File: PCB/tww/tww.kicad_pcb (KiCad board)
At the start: 2 copper layers, 77 x 77 mm, 56 parts, among them J1 MAINS, J10 Flow|NTC, J11 SPI, J2 WW_Pump, J3 Circ_Pump, J6 FtdiConnector, J9 1Wire Sensors, Q1 BC547, Q2 BC547, SW1 Reset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

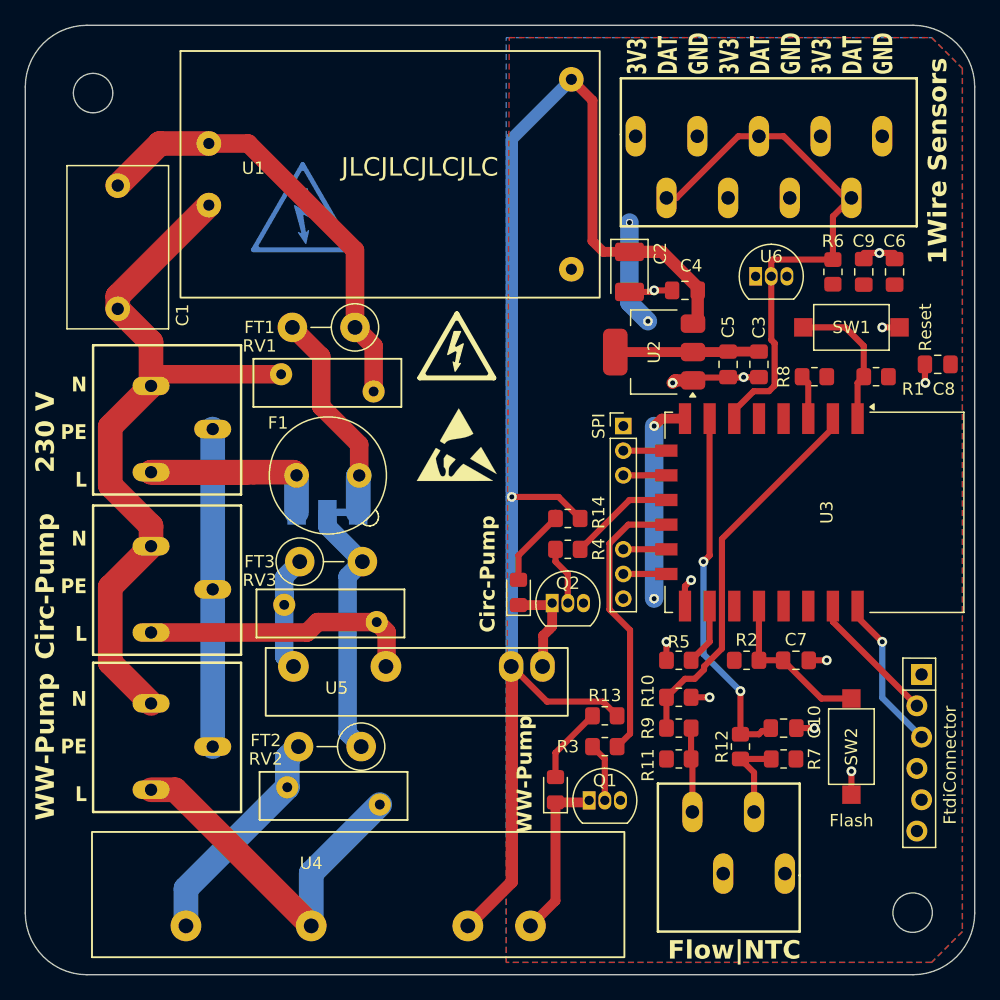
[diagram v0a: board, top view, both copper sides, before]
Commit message: update to PCB v1.1
addresses #1

- U1 (HLK-PM01) output polarity swapped
- J6 (FtdiConnector): RX and TX swapped
- J10 label fixed
- VDR-0.6 footprint changed
- replaced BC547 by FET IRLML6344
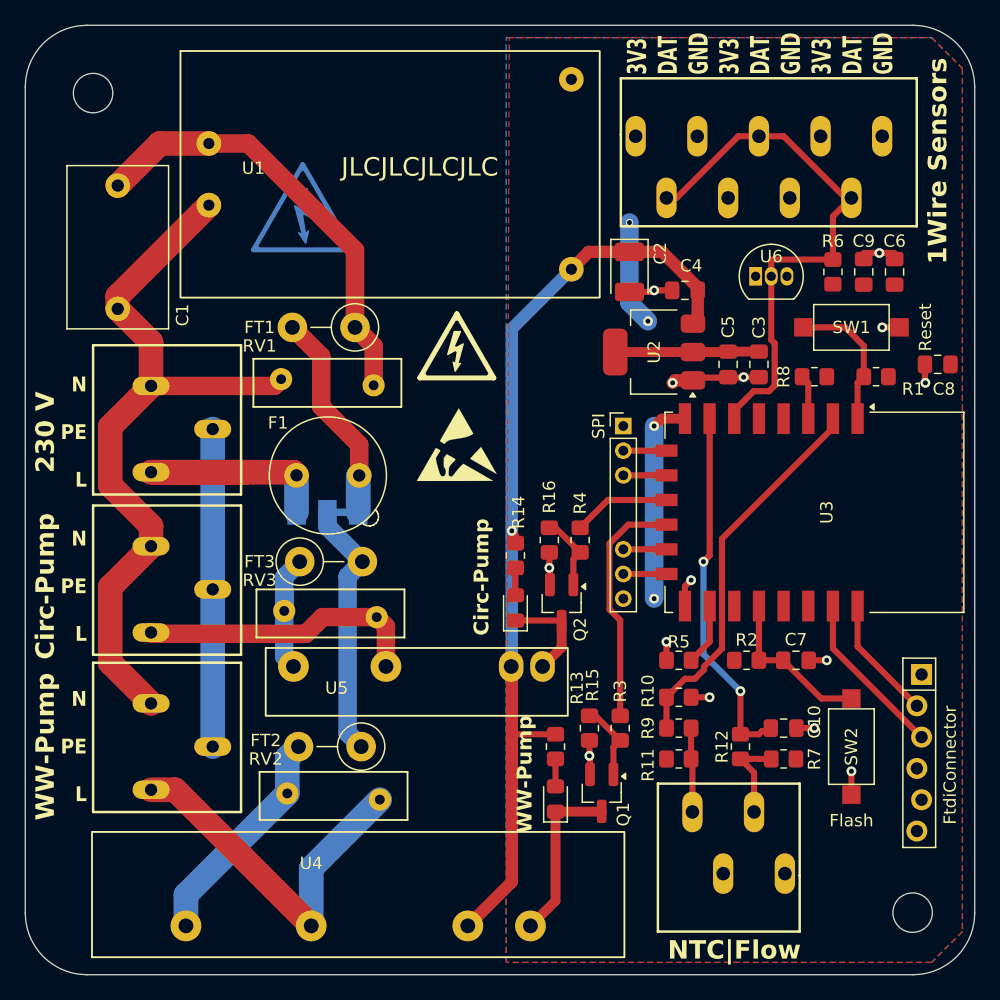
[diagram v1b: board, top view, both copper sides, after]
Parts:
- added R15: 10k, Resistor_SMD:R_0805_2012Metric_Pad1.20x1.40mm_HandSolder, F.Cu at (145.8, 81.0)
- added R16: 10k, Resistor_SMD:R_0805_2012Metric_Pad1.20x1.40mm_HandSolder, F.Cu at (142.5, 65.8)
- J10: value Flow|NTC -> NTC|Flow
- Q1, Q2: value BC547 -> IRLML6344; footprint Package_TO_SOT_THT:TO-92_Inline -> Package_TO_SOT_SMD:SOT-23_Handsoldering
- R13, R14: value 1k? -> 560
- R3, R4: value 1k? -> 300
- moved R14 5.20 mm to (139.8, 67.0), turned to 90 degrees
- moved R13 4.72 mm to (143.0, 82.5), turned to 90 degrees
- moved R3 1.95 mm to (148.2, 81.0), turned to -90 degrees
- moved D2 1.27 mm to (139.8, 71.2)
- moved R4 1.25 mm to (145.0, 65.8), turned to -90 degrees
- moved Q1 1.19 mm to (146.8, 86.2), turned to -90 degrees
- moved Q2 0.77 mm to (143.5, 70.9), turned to -90 degrees
- moved D1 0.75 mm to (143.0, 86.8)
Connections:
- J6 pad 2: /RX -> /TX
- J6 pad 3: /TX -> /RX
- Q1 pad 1: Net-(D1-K) -> Net-(Q1-G)
- Q1 pad 2: Net-(Q1-B) -> GND
- Q1 pad 3: GND -> Net-(D1-K)
- Q2 pad 1: Net-(D2-K) -> Net-(Q2-G)
- Q2 pad 2: Net-(Q2-B) -> GND
- Q2 pad 3: GND -> Net-(D2-K)
- R3 pad 2: Net-(Q1-B) -> Net-(Q1-G)
- R4 pad 2: Net-(Q2-B) -> Net-(Q2-G)
- U1 pad 3: +5V -> GND
- U1 pad 4: GND -> +5V
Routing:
- net +5V: track 115.6 -> 76.6 mm
- net Net-(Q1-G): track 0.00 -> 6.31 mm
- net Net-(Q2-G): track 0.00 -> 6.17 mm
- net GND: track 26.3 -> 31.7 mm, vias 12 -> 14
- net Net-(Q2-B): track 4.77 -> 0.00 mm
- net Net-(Q1-B): track 4.77 -> 0.00 mm
- net Net-(D2-A): track 6.69 -> 2.22 mm
- net Net-(D1-A): track 6.22 -> 2.22 mm
- net /WWP: track 22.9 -> 19.6 mm
- net /TX: track 12.8 -> 10.1 mm, vias 1 -> 0
- net /RX: track 10.9 -> 13.6 mm
- net /L_CIRC: track 22.6 -> 23.4 mm
- net /CIRC: track 8.66 -> 7.93 mm
- net Net-(D1-K): track 13.2 -> 13.9 mm
- net Net-(U1-AC1): track 36.3 -> 35.8 mm
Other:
- board text added: "stan23 10/2024 v1.1 CC BY-NC-SA"
- board text removed: "stan23 10/2024 v1.0 CC BY-NC-SA"

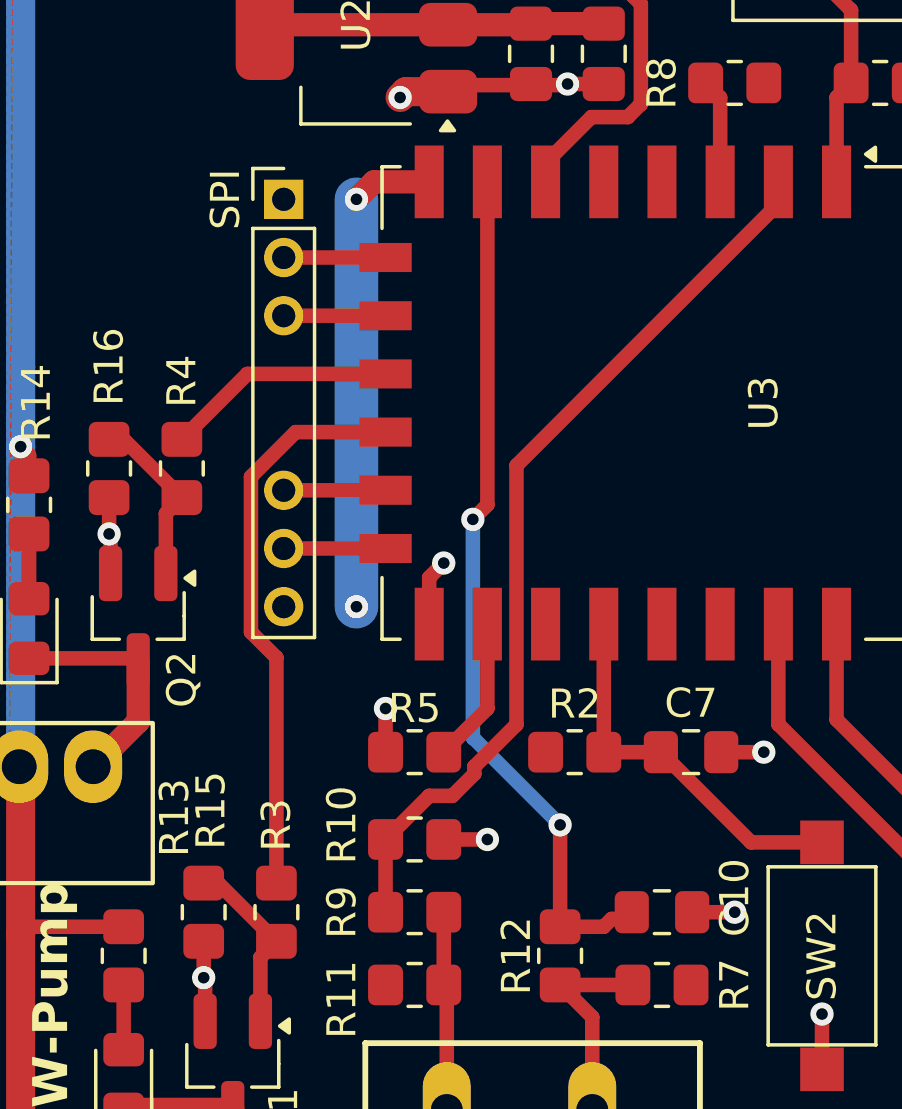
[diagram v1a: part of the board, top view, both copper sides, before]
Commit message: updates for PCB version 1.1
- reconnect WWP and CIRC outputs
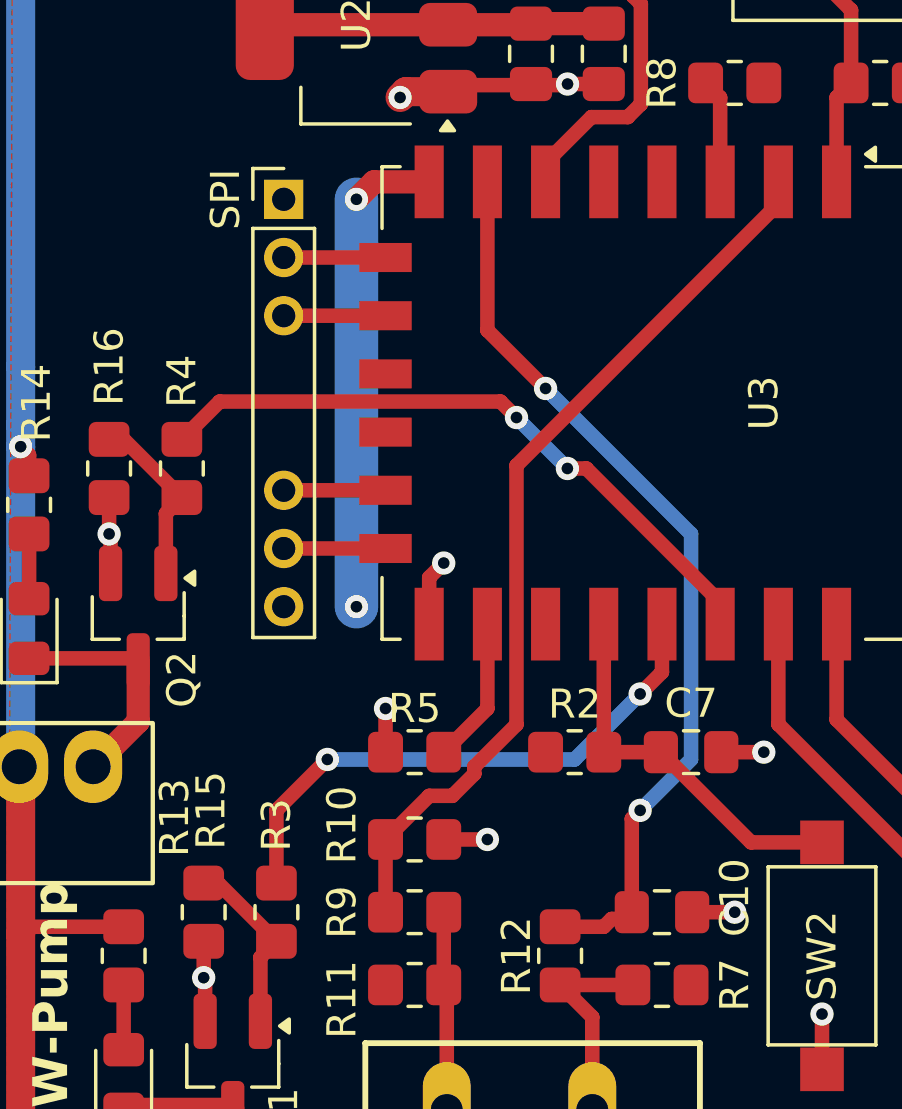
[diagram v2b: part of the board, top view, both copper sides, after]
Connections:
- U3 pad 11: /CIRC -> unconnected-(U3-GPIO9-Pad11)
- U3 pad 12: /WWP -> unconnected-(U3-GPIO10-Pad12)
- U3 pad 19: unconnected-(U3-GPIO4-Pad19) -> /WWP
- U3 pad 20: unconnected-(U3-GPIO5-Pad20) -> /CIRC
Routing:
- net /CIRC: track 7.93 -> 22.6 mm, vias 0 -> 2
- net /FLOW: track 29.7 -> 31.5 mm
- net /WWP: track 19.6 -> 19.4 mm, vias 0 -> 2
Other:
- board text added: "stan23 11/2024 v1.1 CC BY-NC-SA"
- board text removed: "stan23 10/2024 v1.1 CC BY-NC-SA"
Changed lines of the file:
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@@
 	(net 37 "unconnected-(U3-GPIO2-Pad17)")
 	(net 38 "Net-(J10-Pin_2)")
-	(net 39 "unconnected-(U3-GPIO4-Pad19)")
-	(net 40 "unconnected-(U3-GPIO5-Pad20)")
+	(net 39 "unconnected-(U3-GPIO10-Pad12)")
+	(net 40 "unconnected-(U3-GPIO9-Pad11)")
 	(net 41 "/L_SSR")
 	(net 42 "Net-(Q1-G)")
@@
 			(size 1 1.8)
 			(layers "F.Cu" "F.Paste" "F.Mask")
-			(net 10 "/CIRC")
+			(net 40 "unconnected-(U3-GPIO9-Pad11)")
 			(pinfunction "GPIO9")
-			(pintype "bidirectional")
+			(pintype "bidirectional+no_connect")
 		)
 		(pad "12" smd rect
@@
 			(size 1 1.8)
 			(layers "F.Cu" "F.Paste" "F.Mask")
-			(net 9 "/WWP")
+			(net 39 "unconnected-(U3-GPIO10-Pad12)")
 			(pinfunction "GPIO10")
-			(pintype "bidirectional")
+			(pintype "bidirectional+no_connect")
 		)
 		(pad "13" smd rect
@@
 			(size 2.5 1)
 			(layers "F.Cu" "F.Paste" "F.Mask")
-			(net 39 "unconnected-(U3-GPIO4-Pad19)")
+			(net 9 "/WWP")
 			(pinfunction "GPIO4")
-			(pintype "bidirectional+no_connect")
+			(pintype "bidirectional")
 		)
 		(pad "20" smd rect
@@
 			(size 2.5 1)
 			(layers "F.Cu" "F.Paste" "F.Mask")
-			(net 40 "unconnected-(U3-GPIO5-Pad20)")
+			(net 10 "/CIRC")
 			(pinfunction "GPIO5")
-			(pintype "bidirectional+no_connect")
+			(pintype "bidirectional")
 		)
 		(pad "21" smd rect
@@
 		(layer "User.1")
 	)
-	(gr_text "stan23   10/2024   v1.1\nCC BY-NC-SA"
+	(gr_text "stan23   11/2024   v1.1\nCC BY-NC-SA"
 		(at 145.25 48 90)
 		(layer "B.SilkS")
@@
 	)
 	(segment
-		(start 147.375 71.375)
-		(end 147.375 66.034009)
+		(start 148.25 80)
+		(end 148.25 77.5)
 		(width 0.5)
 		(layer "F.Cu")
@@
 	)
 	(segment
-		(start 148.25 72.25)
-		(end 147.375 71.375)
+		(start 161.5 71.1)
+		(end 161.5 72.75)
 		(width 0.5)
 		(layer "F.Cu")
@@
 	)
 	(segment
-		(start 147.375 66.034009)
-		(end 148.909009 64.5)
+		(start 150 75.75)
+		(end 148.25 77.5)
 		(width 0.5)
 		(layer "F.Cu")
@@
 	)
 	(segment
-		(start 148.25 80)
-		(end 148.25 72.25)
+		(start 161.5 72.75)
+		(end 160.75 73.5)
 		(width 0.5)
 		(layer "F.Cu")
 		(net 9)
 	)
+	(via
+		(at 150 75.75)
+		(size 0.8)
+		(drill 0.4)
+		(layers "F.Cu" "B.Cu")
+		(net 9)
+	)
+	(via
+		(at 160.75 73.5)
+		(size 0.8)
+		(drill 0.4)
+		(layers "F.Cu" "B.Cu")
+		(net 9)
+	)
 	(segment
-		(start 148.909009 64.5)
-		(end 152 64.5)
+		(start 158.5 75.75)
+		(end 150 75.75)
 		(width 0.5)
-		(layer "F.Cu")
+		(layer "B.Cu")
+		(net 9)
+	)
+	(segment
+		(start 160.75 73.5)
+		(end 158.5 75.75)
+		(width 0.5)
+		(layer "B.Cu")
 		(net 9)
 	)
 	(segment
-		(start 145 64.75)
-		(end 147.25 62.5)
+		(start 155.95 63.45)
+		(end 146.3 63.45)
+		(width 0.5)
+		(layer "F.Cu")
+		(net 10)
+	)
+	(segment
+		(start 158.9 65.75)
+		(end 158.25 65.75)
+		(width 0.5)
+		(layer "F.Cu")
+		(net 10)
+	)
+	(segment
+		(start 146.3 63.45)
+		(end 145 64.75)
 		(width 0.5)
 		(layer "F.Cu")
@@
 	)
 	(segment
-		(start 147.25 62.5)
-		(end 152 62.5)
+		(start 156.5 64)
+		(end 155.95 63.45)
 		(width 0.5)
 		(layer "F.Cu")
@@
 	)
 	(segment
+		(start 163.5 71.1)
+		(end 163.5 70.35)
+		(width 0.5)
+		(layer "F.Cu")
+		(net 10)
+	)
+	(segment
+		(start 163.5 70.35)
+		(end 158.9 65.75)
+		(width 0.5)
+		(layer "F.Cu")
+		(net 10)
+	)
+	(via
+		(at 158.25 65.75)
+		(size 0.8)
+		(drill 0.4)
+		(layers "F.Cu" "B.Cu")
+		(net 10)
+	)
+	(via
+		(at 156.5 64)
+		(size 0.8)
+		(drill 0.4)
+		(layers "F.Cu" "B.Cu")
+		(net 10)
+	)
+	(segment
+		(start 158.25 65.75)
+		(end 156.5 64)
+		(width 0.5)
+		(layer "B.Cu")
+		(net 10)
+	)
+	(segment
 		(start 139.75 70.225)
 		(end 139.75 68)
@@
 	)
 	(segment
-		(start 155.5 55.9)
-		(end 155.5 67)
+		(start 155.5 61)
+		(end 155.5 55.9)
 		(width 0.5)
 		(layer "F.Cu")
@@
 	)
 	(segment
-		(start 155.5 67)
-		(end 155 67.5)
+		(start 160.4625 81)
+		(end 160.4625 77.7875)
 		(width 0.5)
 		(layer "F.Cu")
@@
 	)
 	(segment
-		(start 158 81.5)
-		(end 158 78)
+		(start 157.5 63)
+		(end 155.5 61)
 		(width 0.5)
 		(layer "F.Cu")
@@
 		(net 31)
 	)
+	(segment
+		(start 160.4625 77.7875)
+		(end 160.75 77.5)
+		(width 0.5)
+		(layer "F.Cu")
+		(net 31)
+	)
 	(via
-		(at 155 67.5)
+		(at 157.5 63)
 		(size 0.8)
 		(drill 0.4)
@@
 	)
 	(via
-		(at 158 78)
+		(at 160.75 77.5)
 		(size 0.8)
 		(drill 0.4)
@@
 	)
 	(segment
-		(start 155 75)
-		(end 158 78)
+		(start 162.5 75.75)
+		(end 160.75 77.5)
+		(width 0.5)
+		(layer "B.Cu")
+		(net 31)
+	)
+	(segment
+		(start 162.5 68)
+		(end 162.5 75.75)
 		(width 0.5)
 		(layer "B.Cu")
@@
 	)
 	(segment
-		(start 155 67.5)
-		(end 155 75)
+		(start 157.5 63)
+		(end 162.5 68)
 		(width 0.5)
 		(layer "B.Cu")
